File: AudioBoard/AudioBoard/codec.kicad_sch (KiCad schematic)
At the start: 9 parts

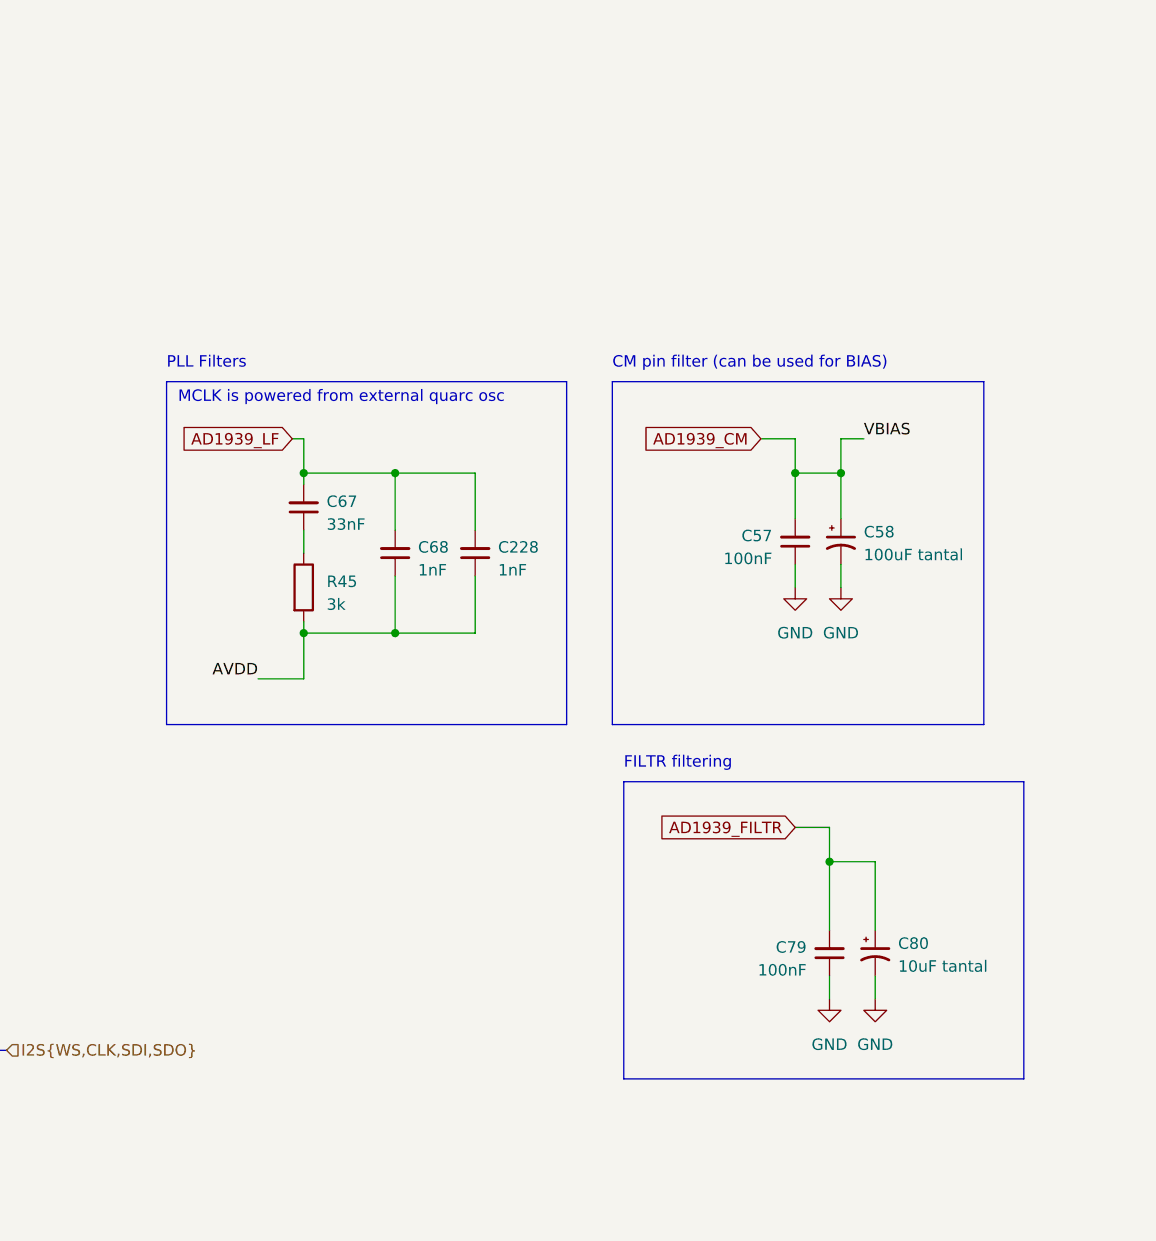
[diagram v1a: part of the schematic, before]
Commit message: modified clamping diodes on inputs, added exp pedal input filter, added ideas to instrument input filter redesign
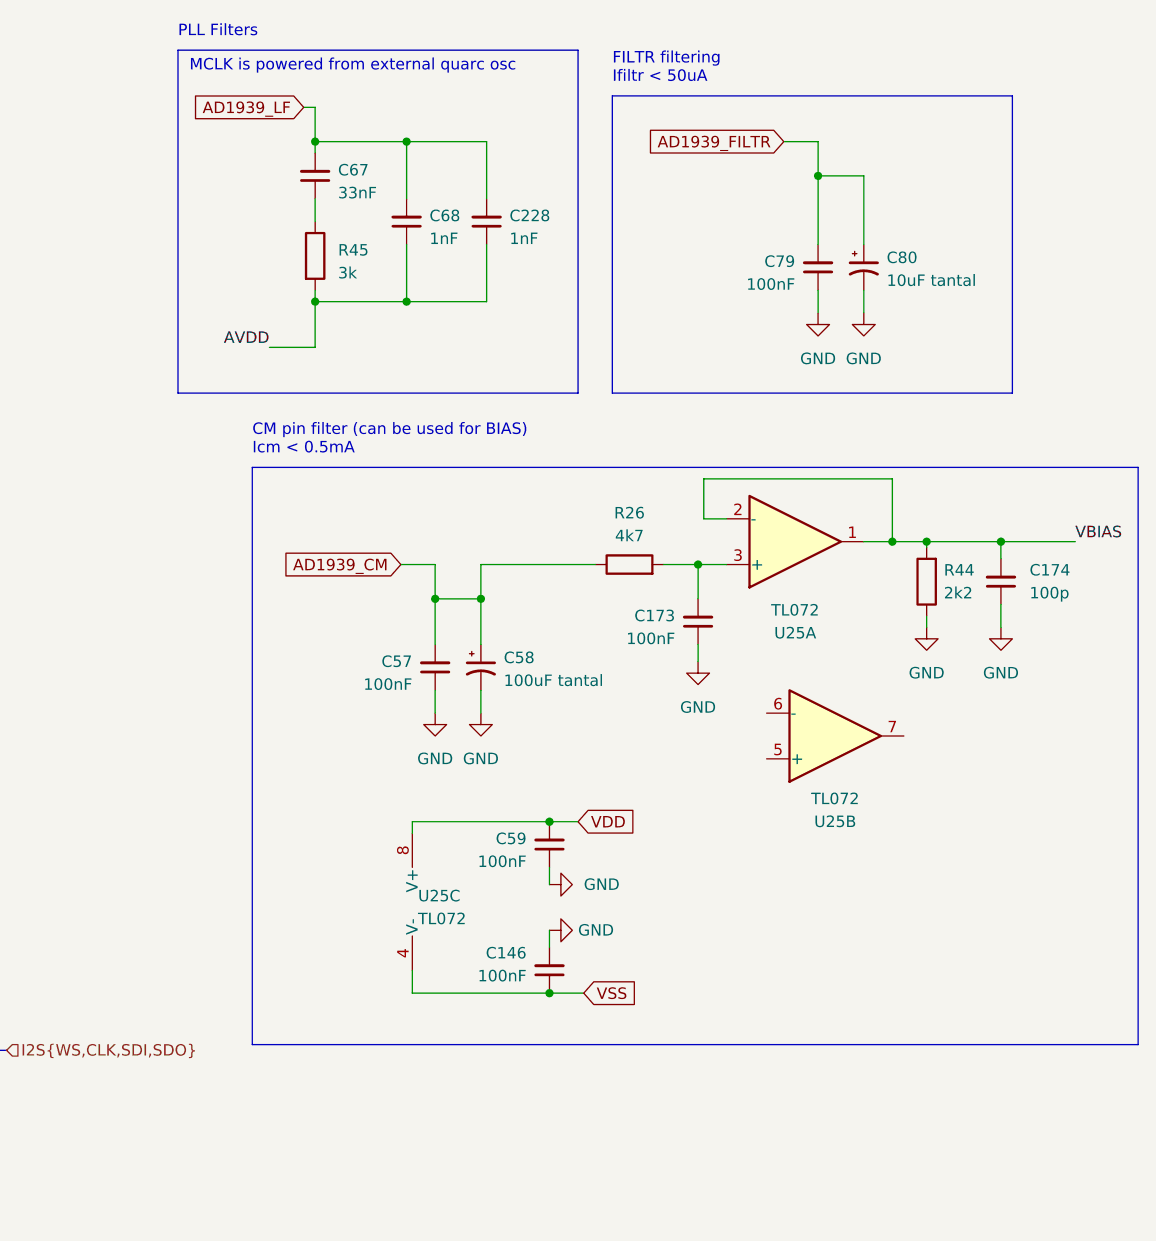
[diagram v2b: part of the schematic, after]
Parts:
- added C146, C173, C59: 100nF, Capacitor_SMD:C_0603_1608Metric, symbol Device:C_Small
- added C174: 100p, Capacitor_SMD:C_0402_1005Metric, symbol Device:C_Small
- added R26: 4k7, Resistor_SMD:R_0402_1005Metric, symbol Device:R
- added R44: 2k2, Resistor_SMD:R_0402_1005Metric, symbol Device:R
- added U25: TL072, Package_SO:SOIC-8_3.9x4.9mm_P1.27mm, symbol Amplifier_Operational:TL072
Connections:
- net AD1939_CM: now also R26.1
- net GND: now also C146.2, C173.1, C174.1, C59.1, R44.1
- new net: C173.2, R26.2, U25.3 (+)
- new net VBIAS: C174.2, R44.2, U25.1, U25.2 (-)
- new net VDD: C59.2, U25.8 (V+)
- new net VSS: C146.1, U25.4 (V-)
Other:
- note added: "CM pin filter (can be used for BIAS) Icm < 0.5mA"
- note added: "FILTR filtering Ifiltr < 50uA"
- note removed: "CM pin filter (can be used for BIAS)"
- note removed: "FILTR filtering"
- moved on the sheet: C228, C57, C58, C67, C68, C79, C80, R45
